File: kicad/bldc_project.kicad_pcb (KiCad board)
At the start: 4 copper layers, 105 x 60 mm, 160 parts, among them J1 Conn_ARM_SWD_TagConnect_TC203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, J2 Screw_Terminal_01x03, J3 Screw_Terminal_01x03, J4 TYPE-C-31-M-12, Q1 IRFZ44N, Q2 IRFZ44N, Q3 IRFZ44N, Q4 IRFZ44N, Q5 IRFZ44N, Q6 IRFZ44N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

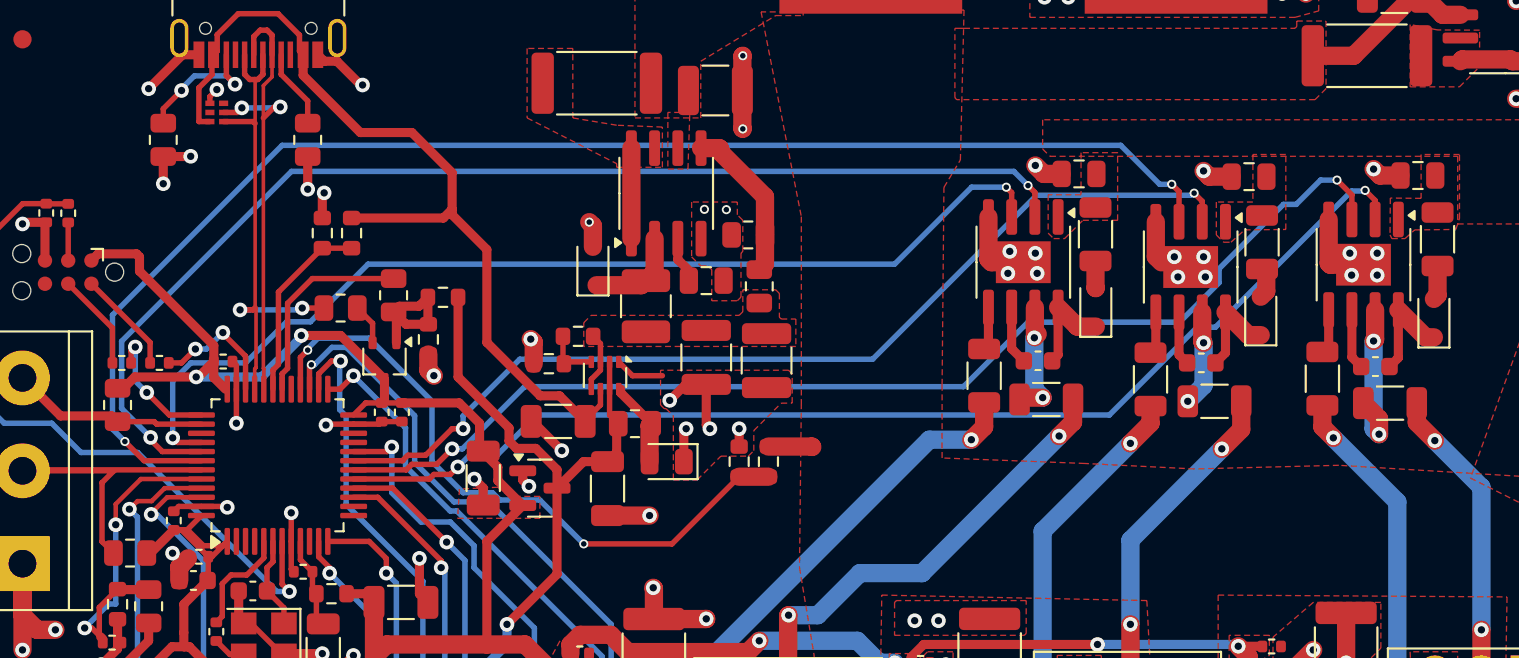
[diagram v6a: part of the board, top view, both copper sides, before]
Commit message: [kicad] TODO: add silkscreen to FET-drivers, tantalum capacitors (check this first), FETs and other polar components OR check with manufacturer
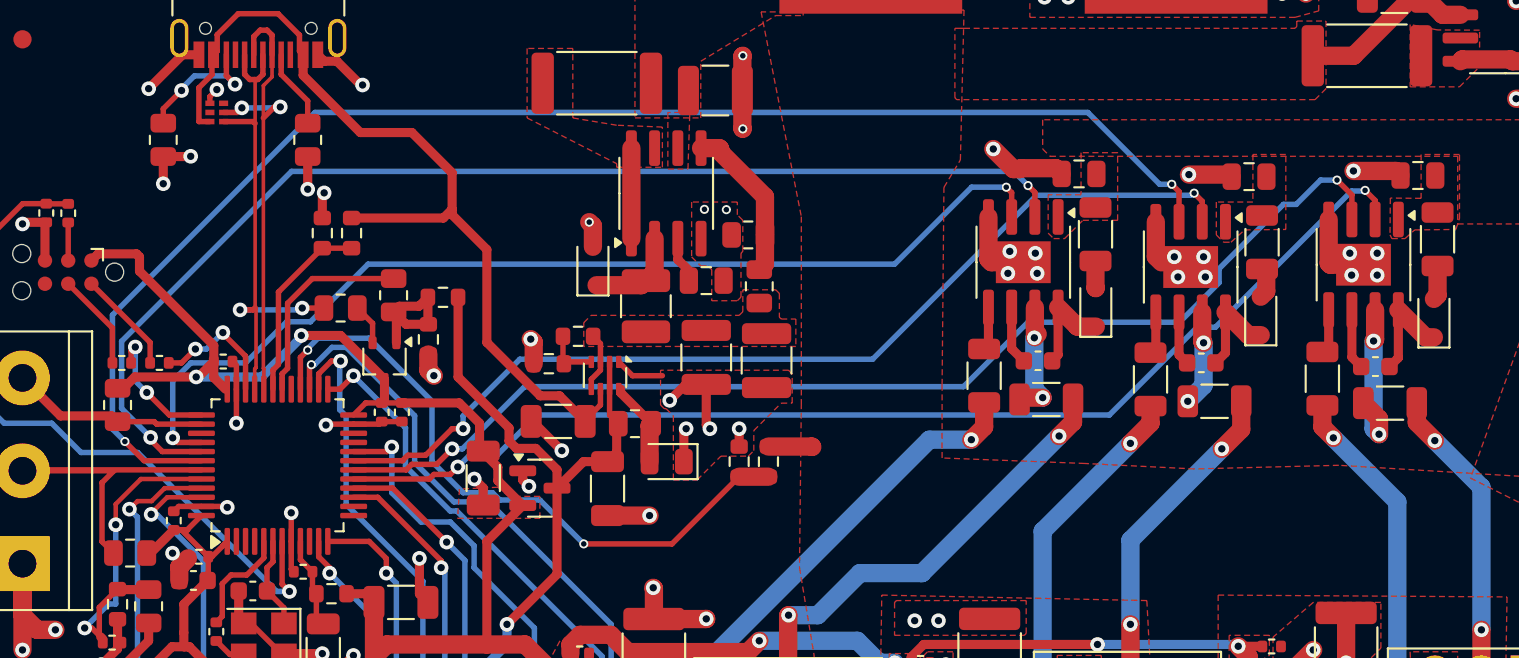
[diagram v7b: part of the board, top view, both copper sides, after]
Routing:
- net GND: track 174.8 -> 179.3 mm
- net +3.3V: track 158.9 -> 156.6 mm
- net PhaseV_SD: track 76.7 -> 78.2 mm
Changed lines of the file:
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@@
   (segment (start 76.1225 130.7175) (end 75.0825 130.7175) (width 0.5) (layer "F.Cu") (net 2))
   (segment (start 110.8 136.175) (end 110.8 134.9) (width 1) (layer "F.Cu") (net 2))
+  (segment (start 111.2275 95.3) (end 111.34 95.4125) (width 1) (layer "F.Cu") (net 2))
   (segment (start 114.165 122.8725) (end 114.2275 122.8725) (width 1) (layer "F.Cu") (net 2))
   (segment (start 116.645 97.755) (end 116.645 100.145) (width 1) (layer "F.Cu") (net 2))
@@
   (segment (start 79.7375 119.61) (end 82.59 119.61) (width 1) (layer "F.Cu") (net 2))
   (segment (start 55.15 127.95) (end 55.15 127.425) (width 0.3) (layer "F.Cu") (net 2))
+  (segment (start 101.7275 94.95) (end 102.04 95.2625) (width 1) (layer "F.Cu") (net 2))
   (segment (start 117 85.1) (end 115.7 85.1) (width 1) (layer "F.Cu") (net 2))
   (segment (start 78.5675 106.3) (end 80.2 106.3) (width 0.3) (layer "F.Cu") (net 2))
   (segment (start 79.7375 119.61) (end 79.7375 117.9375) (width 1) (layer "F.Cu") (net 2))
-  (segment (start 120.575 95.35) (end 119.45 95.35) (width 1) (layer "F.Cu") (net 2))
   (segment (start 56.9 105.74) (end 56.9 107.0375) (width 0.3) (layer "F.Cu") (net 2))
   (segment (start 76.4 98.1) (end 76.2 97.9) (width 1) (layer "F.Cu") (net 2))
@@
   (segment (start 61.65 122.825) (end 62.075 122.825) (width 0.5) (layer "F.Cu") (net 2))
   (segment (start 98.035 99.935) (end 98.1925 100.0925) (width 1) (layer "F.Cu") (net 2))
-  (segment (start 102.04 95.2625) (end 101.0625 95.2625) (width 1) (layer "F.Cu") (net 2))
   (segment (start 46.5 97.91) (end 45.29 97.91) (width 0.5) (layer "F.Cu") (net 2))
   (segment (start 74.9 134.025) (end 74.9 134.8) (width 0.5) (layer "F.Cu") (net 2))
@@
   (segment (start 56.35 113.45) (end 56.4 113.5) (width 0.3) (layer "F.Cu") (net 2))
   (segment (start 128.68 128.5) (end 129.8 128.5) (width 0.25) (layer "F.Cu") (net 2))
-  (segment (start 111.34 95.4125) (end 110.1125 95.4125) (width 1) (layer "F.Cu") (net 2))
   (segment (start 47 120.2) (end 46 120.2) (width 1) (layer "F.Cu") (net 2))
   (segment (start 113.215 126.685) (end 113.1 126.8) (width 0.5) (layer "F.Cu") (net 2))
@@
   (segment (start 52.9 94.3125) (end 54.3875 94.3125) (width 0.5) (layer "F.Cu") (net 2))
   (segment (start 52.9 94.3125) (end 52.9 95.8) (width 0.5) (layer "F.Cu") (net 2))
+  (segment (start 118 95.1) (end 120.325 95.1) (width 1) (layer "F.Cu") (net 2))
   (segment (start 91.7825 128.8175) (end 91.8 128.8) (width 0.5) (layer "F.Cu") (net 2))
   (segment (start 52.402083 123.3) (end 53.3 123.3) (width 0.3) (layer "F.Cu") (net 2))
@@
   (segment (start 57.7 119.85) (end 59.4 121.55) (width 0.3) (layer "F.Cu") (net 2))
   (segment (start 63.7 90.4) (end 62.4 89.1) (width 0.5) (layer "F.Cu") (net 2))
+  (segment (start 99.756497 95) (end 99.806497 94.95) (width 1) (layer "F.Cu") (net 2))
   (segment (start 64.85 108.81) (end 64.71 108.95) (width 0.3) (layer "F.Cu") (net 2))
   (segment (start 98.1925 100.0925) (end 99.94 100.0925) (width 1) (layer "F.Cu") (net 2))
@@
   (segment (start 91.3 132.6) (end 91.2575 132.5575) (width 0.5) (layer "F.Cu") (net 2))
   (segment (start 53.3 123.3) (end 53.3 122.6) (width 0.3) (layer "F.Cu") (net 2))
+  (segment (start 120.325 95.1) (end 120.575 95.35) (width 1) (layer "F.Cu") (net 2))
   (segment (start 129.68457 85.29) (end 131.02457 83.95) (width 1) (layer "F.Cu") (net 2))
+  (segment (start 99.806497 94.95) (end 101.7275 94.95) (width 1) (layer "F.Cu") (net 2))
   (segment (start 77.8125 105.545) (end 78.5675 106.3) (width 0.3) (layer "F.Cu") (net 2))
   (segment (start 79.5 113.95) (end 77.2 113.95) (width 1) (layer "F.Cu") (net 2))
-  (segment (start 110.1125 95.4125) (end 109.8 95.1) (width 1) (layer "F.Cu") (net 2))
   (segment (start 127.29 85.41) (end 126.9 85.8) (width 1) (layer "F.Cu") (net 2))
+  (segment (start 109 95.3) (end 111.2275 95.3) (width 1) (layer "F.Cu") (net 2))
   (segment (start 75.6175 126.5825) (end 75.1 127.1) (width 0.5) (layer "F.Cu") (net 2))
   (segment (start 54.9875 113.45) (end 56.35 113.45) (width 0.3) (layer "F.Cu") (net 2))
@@
   (segment (start 84.575 90.7) (end 84.575 92.775) (width 1) (layer "F.Cu") (net 2))
   (segment (start 55.15 127.425) (end 54.175 126.45) (width 0.3) (layer "F.Cu") (net 2))
+  (segment (start 98.3 93.9) (end 99.4 95) (width 1) (layer "F.Cu") (net 2))
   (segment (start 128.8 85.29) (end 128.68 85.41) (width 1) (layer "F.Cu") (net 2))
   (segment (start 114.2275 122.8725) (end 115.8 121.3) (width 1) (layer "F.Cu") (net 2))
@@
   (segment (start 64.71 108.95) (end 63.3125 108.95) (width 0.3) (layer "F.Cu") (net 2))
   (segment (start 57.025 118.075) (end 57.025 119.575) (width 0.5) (layer "F.Cu") (net 2))
-  (segment (start 119.45 95.35) (end 119.1 95) (width 1) (layer "F.Cu") (net 2))
-  (segment (start 101.0625 95.2625) (end 100.6 94.8) (width 1) (layer "F.Cu") (net 2))
+  (segment (start 99.4 95) (end 99.756497 95) (width 1) (layer "F.Cu") (net 2))
   (segment (start 61.6 121.5) (end 59.55 121.5) (width 0.5) (layer "F.Cu") (net 2))
   (segment (start 90.7375 128.8175) (end 91.7825 128.8175) (width 0.5) (layer "F.Cu") (net 2))
@@
   (via (at 139.1 103.7) (size 0.8) (drill 0.4) (layers "F.Cu" "B.Cu") (free) (net 2))
   (via (at 140.1 126.2) (size 0.8) (drill 0.4) (layers "F.Cu" "B.Cu") (free) (net 2))
-  (via (at 119.1 95) (size 0.8) (drill 0.4) (layers "F.Cu" "B.Cu") (net 2))
+  (via (at 118 95.1) (size 0.8) (drill 0.4) (layers "F.Cu" "B.Cu") (net 2))
   (via (at 102.4 85.6) (size 0.8) (drill 0.4) (layers "F.Cu" "B.Cu") (free) (net 2))
   (via (at 84.4 109.2) (size 0.8) (drill 0.4) (layers "F.Cu" "B.Cu") (net 2))
@@
   (via (at 129.8 128.5) (size 0.8) (drill 0.4) (layers "F.Cu" "B.Cu") (net 2))
   (via (at 102.4 82.1) (size 0.8) (drill 0.4) (layers "F.Cu" "B.Cu") (free) (net 2))
-  (via (at 109.8 95.1) (size 0.8) (drill 0.4) (layers "F.Cu" "B.Cu") (net 2))
+  (via (at 109 95.3) (size 0.8) (drill 0.4) (layers "F.Cu" "B.Cu") (net 2))
   (via (at 91.3 132.6) (size 0.8) (drill 0.4) (layers "F.Cu" "B.Cu") (net 2))
   (via (at 140.1 104.3) (size 0.8) (drill 0.4) (layers "F.Cu" "B.Cu") (free) (net 2))
@@
   (via (at 72.9 112.35) (size 0.8) (drill 0.4) (layers "F.Cu" "B.Cu") (net 2))
   (via (at 53.406041 116.006041) (size 0.8) (drill 0.4) (layers "F.Cu" "B.Cu") (net 2))
-  (via (at 100.6 94.8) (size 0.8) (drill 0.4) (layers "F.Cu" "B.Cu") (net 2))
+  (via (at 98.3 93.9) (size 0.8) (drill 0.4) (layers "F.Cu" "B.Cu") (net 2))
   (segment (start 119.975 105.8) (end 120.455 105.32) (width 0.5) (layer "F.Cu") (net 3))
   (segment (start 120.455 105.32) (end 120.455 102.705) (width 0.5) (layer "F.Cu") (net 3))
@@
   (segment (start 86 110.175) (end 88.375 110.175) (width 1) (layer "F.Cu") (net 17))
   (segment (start 115.775 88.8) (end 118.0125 88.8) (width 1) (layer "F.Cu") (net 17))
-  (segment (start 55.1 115.6) (end 56.1625 115.6) (width 0.3) (layer "F.Cu") (net 18))
   (segment (start 93.7975 122) (end 93.8075 122.01) (width 0.5) (layer "F.Cu") (net 18))
   (segment (start 70.6 115.3625) (end 70.6 121) (width 0.5) (layer "F.Cu") (net 18))
@@
   (segment (start 55.665 104.646776) (end 51.6 100.581776) (width 0.5) (layer "F.Cu") (net 18))
   (segment (start 51.6 99.8) (end 51.4357 99.6357) (width 0.5) (layer "F.Cu") (net 18))
-  (segment (start 54.235 114.735) (end 55.1 115.6) (width 0.3) (layer "F.Cu") (net 18))
   (segment (start 62.6 104.1) (end 65 106.5) (width 0.5) (layer "F.Cu") (net 18))
   (segment (start 112.265 121.665) (end 111.7 121.1) (width 1) (layer "F.Cu") (net 18))
@@
   (via (at 108.060576 95.83) (size 0.5) (drill 0.3) (layers "F.Cu" "B.Cu") (net 81))
   (via (at 50.8 109.9) (size 0.5) (drill 0.3) (layers "F.Cu" "B.Cu") (net 81))
-  (segment (start 107.4 95.83) (end 105.27 93.7) (width 0.3) (layer "B.Cu") (net 81))
   (segment (start 50.119669 109.219669) (end 50.8 109.9) (width 0.3) (layer "B.Cu") (net 81))
+  (segment (start 107.4 95.83) (end 103.47 91.9) (width 0.3) (layer "B.Cu") (net 81))
+  (segment (start 50.119669 102.980331) (end 50.119669 109.219669) (width 0.3) (layer "B.Cu") (net 81))
   (segment (start 108.060576 95.83) (end 107.4 95.83) (width 0.3) (layer "B.Cu") (net 81))
-  (segment (start 105.27 93.7) (end 59.4 93.7) (width 0.3) (layer "B.Cu") (net 81))
-  (segment (start 50.119669 102.980331) (end 50.119669 109.219669) (width 0.3) (layer "B.Cu") (net 81))
-  (segment (start 59.4 93.7) (end 50.119669 102.980331) (width 0.3) (layer "B.Cu") (net 81))
+  (segment (start 61.2 91.9) (end 50.119669 102.980331) (width 0.3) (layer "B.Cu") (net 81))
+  (segment (start 103.47 91.9) (end 61.2 91.9) (width 0.3) (layer "B.Cu") (net 81))
   (segment (start 100.575 96.275) (end 100.575 97.6175) (width 0.3) (layer "F.Cu") (net 82))
   (segment (start 52.85 110.45) (end 52.207719 109.807719) (width 0.3) (layer "F.Cu") (net 82))

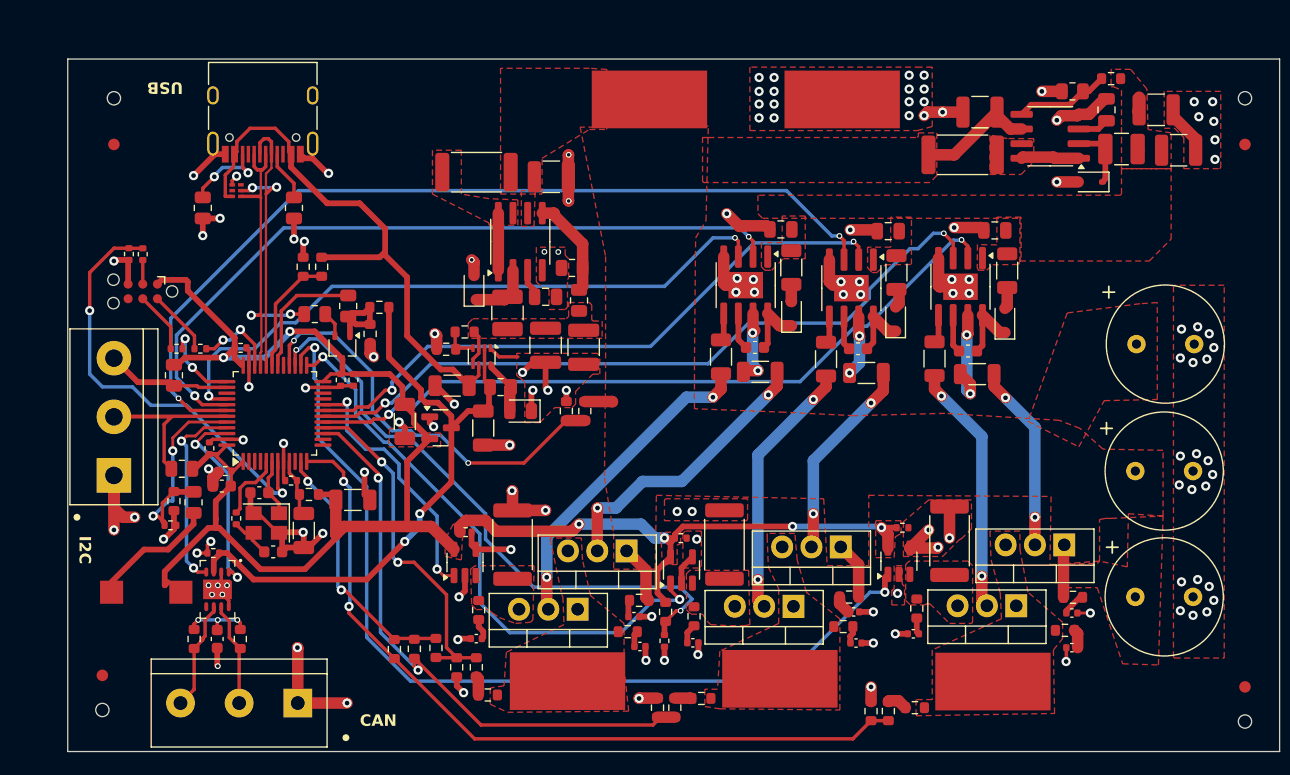
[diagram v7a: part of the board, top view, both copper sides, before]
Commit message: [bldc] Added cathode indicators and capacitor polarity indicators | TODO: Check screw terminal pads, check for appropriate 3d model, check 3d model for button
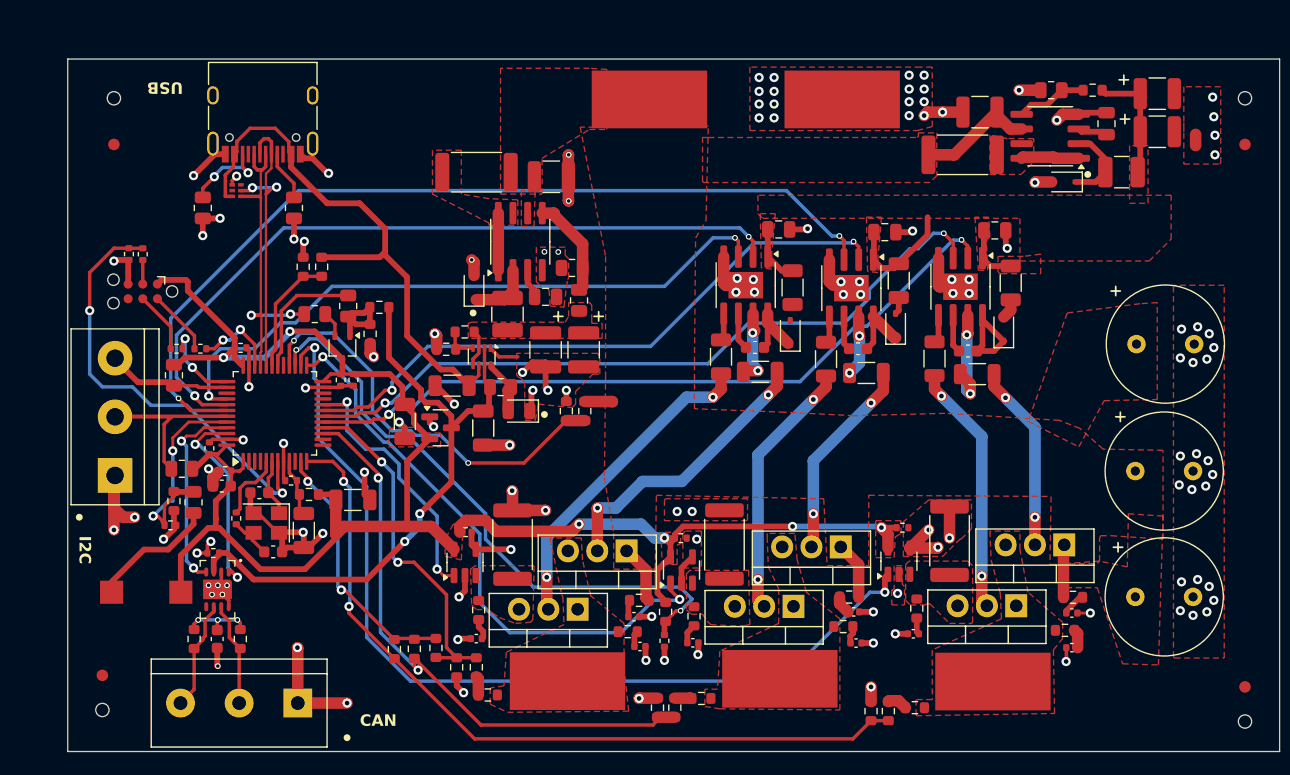
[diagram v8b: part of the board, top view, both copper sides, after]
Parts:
- moved C41 5.24 mm to (135.6, 83.5)
- moved D8 2.30 mm to (127.5, 91.2)
- moved L2 2.00 mm to (132.5, 90.3)
- moved C39 1.90 mm to (135.6, 86.8)
- moved R48 1.89 mm to (130.0, 83.2)
- moved R55 1.84 mm to (126.4, 83.2)
- moved R3 1.74 mm to (104.0, 100.3)
- moved D3 1.64 mm to (103.8, 104.2)
- moved C43 1.20 mm to (131.2, 86.1)
- moved R1 1.10 mm to (122.9, 99.9)
- moved D1 0.76 mm to (122.3, 103.9)
- moved R2 0.73 mm to (113.2, 99.7)
- moved D2 0.57 mm to (112.9, 103.6)
- moved C40 0.40 mm to (82.6, 105.7)
- moved C2 0.30 mm to (112.0, 95.5), turned to 0 degrees
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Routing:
- net +10V: track 1.42 -> 30.6 mm
- net GND: track 179.3 -> 170.4 mm, vias 130 -> 128
- net Net-(D1-K): track 5.86 -> 8.98 mm
- net Net-(U11-Vfb): track 8.20 -> 6.70 mm
- net Net-(D3-A): track 1.49 -> 0.00 mm
- net Net-(D8-K): track 5.53 -> 6.90 mm
- net Net-(D3-K): track 5.55 -> 6.34 mm
- net +3.3V: track 156.6 -> 156.0 mm
